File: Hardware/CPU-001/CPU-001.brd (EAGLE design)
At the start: 39.4 x 39.4 mm, 73 parts, among them IC1 IS42S16800F-7TL, J1 10144517-042802LF, J2 10144518-041802LF, J3 10144517-042802LF, J4 10144518-041802LF, J6 2X5_0.05_SWD, U1 ATSAMV71Q19B-AABT, U2 ATA6561-GAQW-N, U6 NCV8170AXV330T2G, U7 ATA6561-GAQW-N

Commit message: more work on CPU-001
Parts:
- added C21: 1uF, rcl:C0603
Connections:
- removed net +3.5V: C1.1, J3.31, J3.33, J3.35, J3.37, J4.31, J4.33, J4.35, J4.37, U6.1, U6.6
- removed net CAN2_N: R39.1, U2.6
- removed net CAN2_P: R39.2, U2.7
- removed net CANRX2: U2.4
- removed net CANTX2: U2.1
- removed net CAN_N: J1.6, J2.6
- removed net CAN_P: J1.4, J2.4
- removed net CAN_STBY2: U2.8
- removed net RFU_3: J1.3, J2.3
- removed net RFU_5: J1.5, J2.5
- removed net RFU_7: J1.7, J2.7
- new net +12V: J3.17, J3.19, J3.21, J3.23, J3.25, J3.27, J3.29, J4.17, J4.19, J4.21, J4.23, J4.25, J4.27, J4.29
- new net CAN0_N: J1.6, J2.6, R26999.1, U7.6
- new net CAN0_P: J1.4, J2.4, R26999.2, U7.7
- new net CANRX0: U7.4
- new net CANTX0: U7.1
- new net CAN_STBY0: U7.8
- net +3V3: now also C21.1, U$5.4
- net +5V: now also C1.1, J3.31, J3.33, J3.35, J3.37, J4.31, J4.33, J4.35, J4.37, U6.1, U6.6; no longer J3.17, J3.19, J3.21, J3.23, J3.25, J3.27, J3.29, J4.17, J4.19, J4.21, J4.23, J4.25, J4.27, J4.29
- net CAN1_N: now also J1.5, J2.5, R39.1, U2.6; no longer R26999.1, U7.6
- net CAN1_P: now also J1.3, J2.3, R39.2, U2.7; no longer R26999.2, U7.7
- net CANRX1: now also U2.4; no longer U7.4
- net CANTX1: now also U2.1; no longer U7.1
- net CAN_STBY1: now also U2.8; no longer U7.8
- net GND: now also C21.2, U$5.6, U$5.MT1, U$5.MT2
- net PA25: now also U$5.5
- net PA26: now also U$5.1
- net PA27: now also U$5.2
- net PA28: now also U$5.3
- net PA30: now also U$5.7
- net PA31: now also U$5.8
- net SHIELD: now also J1.7, J2.7
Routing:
- net CAN_P: track 9.77 -> 0.00 mm, vias 1 -> 0
- net CAN_N: track 9.57 -> 0.00 mm, vias 1 -> 0
- net CAN0_P: track 0.00 -> 8.20 mm, vias 0 -> 1
- net CAN0_N: track 0.00 -> 8.00 mm, vias 0 -> 1
- net RFU_7: track 3.07 -> 0.00 mm, vias 1 -> 0
- net RFU_5: track 3.07 -> 0.00 mm, vias 1 -> 0
- net RFU_3: track 3.07 -> 0.00 mm, vias 1 -> 0
- net CAN1_P: track 0.00 -> 1.44 mm, vias 0 -> 1
- net CAN1_N: track 0.00 -> 1.44 mm, vias 0 -> 1

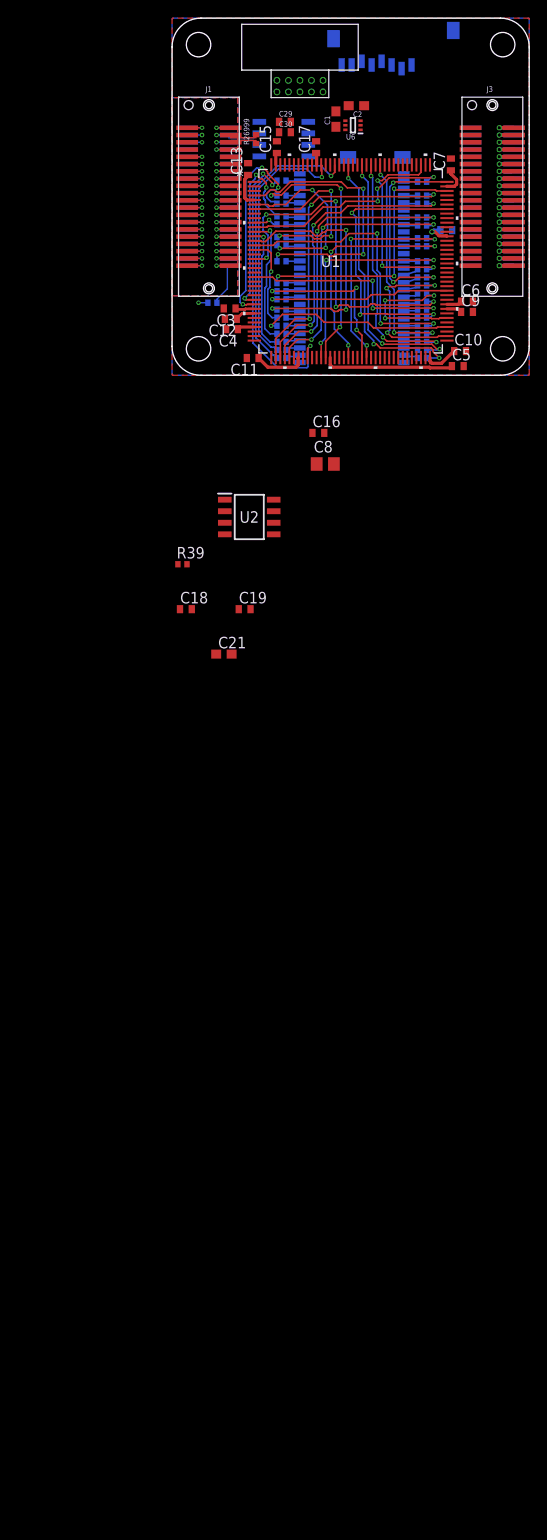
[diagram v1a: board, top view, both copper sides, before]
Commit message: added altimeter.. working through schematic slowly...
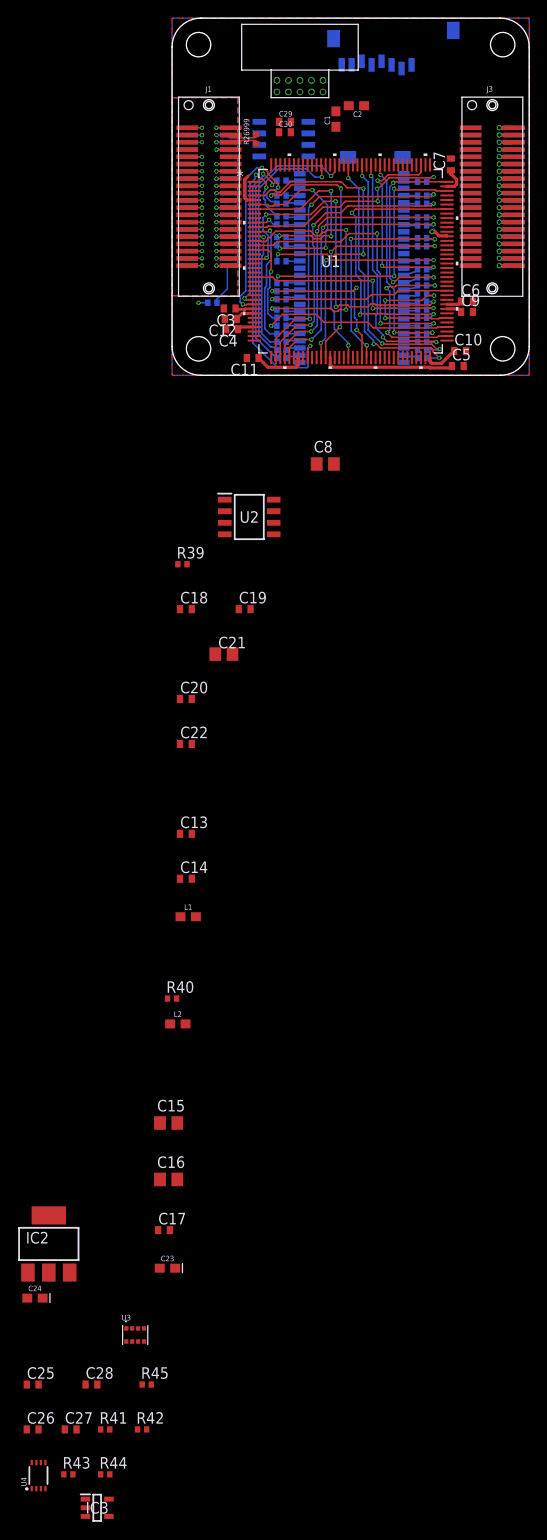
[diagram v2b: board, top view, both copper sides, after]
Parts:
- removed U6: NCV8170AXV330T2G, SamacSys_Parts:SOTFL50P160X60-6N
- added C20: 1u, rcl:C0402
- added C22: 100n, rcl:C0402
- added C23, C24: 10uF, SparkFun-Capacitors:0603-POLAR
- added C25, C28: 100nF, rcl:C0402
- added C26, C27: 1uF, rcl:C0402
- added IC2: NCV1117ST33T3G, v-reg:SOT223
- added IC3: TLV71318PQDBVRQ1, SamacSys_Parts:SOT95P280X100-5N
- added L1, L2: 470@100MHz, SparkFun-Coils:0603
- added R40, R43, R44: (no value), rcl:R0402
- added R41, R42: 10k, rcl:R0402
- added R45: 200k, rcl:R0402
- added U3: ICP-10111, ICP-10111:PSON65P250X200X100-8N
- added U4: PCA9306, SparkFun-IC-Comms:PCA9306DC
- C15, C16: value 100n -> 4.7u; device rcl:C0402 -> rcl:C0805
- C21: value 1uF -> 4.7u; device rcl:C0603 -> rcl:C0805
- C8: value 10u -> 4.7u
- moved C17 120.6 mm to (-0.89, -94.2), turned to 0 degrees
- moved C15 108.2 mm to (-0.38, -82.4), turned to 0 degrees
- moved C16 83.9 mm to (-0.38, -88.6)
- moved C14 77.0 mm to (1.52, -55.5), flipped to the top, turned to 0 degrees
- moved C13 73.6 mm to (1.52, -50.5), turned to 0 degrees
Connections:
- removed net CANRX0: U7.4
- removed net CANRX1: U2.4
- removed net CANTX0: U7.1
- removed net CANTX1: U2.1
- removed net CAN_STBY0: U7.8
- removed net CAN_STBY1: U2.8
- removed net N$2: C3.1, C4.1, C5.1, C6.1, C7.1, U1.107, U1.29, U1.33, U1.50, U1.81
- removed net N$3: C10.1, C11.1, C12.1, C13.1, C14.1, C15.1, C16.1, C17.1, C8.1, C9.1, U1.134, U1.143, U1.30, U1.43, U1.5, U1.72, U1.80, U1.96
- removed net VDDTUMIC: U1.139
- new net +1.8V: C25.1, C27.1, IC3.4, IC3.5, R41.2, R42.2, U3.8, U4.1
- new net N$1: C28.1, R45.2, U4.7, U4.8
- new net N$4: L2.1, R40.2
- new net SCL0_1V8: R42.1, U3.4, U4.2
- new net SDA0_1V8: R41.1, U3.3, U4.3
- new net VDDOUT: C17.1, C20.1, C22.1, C3.1, C4.1, C5.1, C6.1, C7.1, L1.1, U1.107, U1.139, U1.29, U1.3, U1.33, U1.50, U1.81
- new net VDDPLLUSB: C16.1, L2.2, U1.143
- net +3V3: now also C10.1, C11.1, C12.1, C13.1, C14.1, C23.+, C26.1, C8.1, C9.1, IC2.4, IC3.1, IC3.3, R40.1, R43.2, R44.2, R45.1, U1.134, U1.30, U1.43, U1.5, U1.72, U1.80, U1.96; no longer U6.3
- net +5V: now also C24.+, IC2.3; no longer U6.1, U6.6
- net GND: now also C20.2, C22.2, C23.-, C24.-, C25.2, C26.2, C27.2, C28.2, IC2.1, IC3.2, U3.1, U3.2, U3.5, U3.6, U3.7, U4.4; no longer U6.2, U6.5
- net PA1: now also U7.8
- net PA2: now also U2.8
- net PA3: now also R43.1, U4.5
- net PA4: now also R44.1, U4.6
- net PB2: now also U7.1
- net PB3: now also U7.4
- net PC12: now also U2.4
- net PC14: now also U2.1
- net VDDPLL: now also C15.1, L1.2
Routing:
- net VDDOUT: track 0.00 -> 23.1 mm
- net N$2: track 23.1 -> 0.00 mm
- net N$3: track 22.7 -> 0.00 mm, vias 1 -> 0
- net +3V3: track 0.00 -> 19.2 mm, vias 0 -> 1

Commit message: updates to CPU-001 and DBG-001
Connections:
- net +3V3: now also IC1.1, IC1.14, IC1.27, IC1.3, IC1.43, IC1.49, IC1.9
- net GND: now also IC1.12, IC1.28, IC1.41, IC1.46, IC1.52, IC1.54, IC1.6
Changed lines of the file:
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@@
 <contactref element="C27" pad="2"/>
 <contactref element="C28" pad="2"/>
+<contactref element="IC1" pad="6"/>
+<contactref element="IC1" pad="12"/>
+<contactref element="IC1" pad="54"/>
+<contactref element="IC1" pad="28"/>
+<contactref element="IC1" pad="41"/>
+<contactref element="IC1" pad="46"/>
+<contactref element="IC1" pad="52"/>
 <wire x1="-9.555" y1="-124.841" x2="-13.962" y2="-122.7312" width="0" layer="19" extent="1-1"/>
 <wire x1="-14.717" y1="-116.205" x2="-13.962" y2="-122.7312" width="0" layer="19" extent="1-1"/>
@@
 <wire x1="5.809" y1="-14.986" x2="8.651" y2="-25.781" width="0" layer="19" extent="1-1"/>
 <wire x1="17.841" y1="-9.779" x2="5.809" y2="-14.986" width="0" layer="19" extent="1-1"/>
-<wire x1="14.435" y1="1.9558" x2="17.841" y2="-9.779" width="0" layer="19" extent="1-1"/>
-<wire x1="8.24" y1="1.905" x2="14.435" y2="1.9558" width="0" layer="19" extent="1-1"/>
+<wire x1="14.084" y1="1.411" x2="17.841" y2="-9.779" width="0" layer="19" extent="1-16"/>
+<wire x1="14.435" y1="1.9558" x2="14.084" y2="1.411" width="0" layer="19" extent="1-16"/>
+<wire x1="8.24" y1="1.905" x2="14.084" y2="1.411" width="0" layer="19" extent="1-16"/>
 <wire x1="5.954" y1="5.08" x2="8.24" y2="1.905" width="0" layer="19" extent="1-1"/>
 <wire x1="5.827" y1="6.223" x2="5.954" y2="5.08" width="0" layer="19" extent="1-1"/>
@@
 <wire x1="30.734" y1="23.891" x2="36.068" y2="24.085" width="0" layer="19" extent="1-1"/>
 <wire x1="25.435" y1="23.1902" x2="30.734" y2="23.891" width="0" layer="19" extent="1-1"/>
-<wire x1="30.3022" y1="14.823" x2="36.068" y2="14.485" width="0" layer="19" extent="1-1"/>
+<wire x1="25.54" y1="18.211" x2="25.435" y2="23.1902" width="0" layer="19" extent="1-16"/>
+<wire x1="25.54" y1="13.411" x2="25.54" y2="18.211" width="0" layer="19" extent="16-16"/>
+<wire x1="30.3022" y1="14.823" x2="25.54" y2="13.411" width="0" layer="19" extent="1-16"/>
 <wire x1="19.47" y1="29.718" x2="25.435" y2="23.1902" width="0" layer="19" extent="1-1"/>
 <wire x1="18.0594" y1="29.0948" x2="19.47" y2="29.718" width="0" layer="19" extent="1-1"/>
@@
 <wire x1="15.435" y1="23.1902" x2="15.019" y2="26.67" width="0" layer="19" extent="1-16"/>
 <wire x1="13.935" y1="23.1902" x2="15.435" y2="23.1902" width="0" layer="19" extent="1-1"/>
+<wire x1="14.084" y1="22.211" x2="13.935" y2="23.1902" width="0" layer="19" extent="1-16"/>
+<wire x1="14.084" y1="20.611" x2="14.084" y2="22.211" width="0" layer="19" extent="16-16"/>
+<wire x1="14.084" y1="15.811" x2="14.084" y2="20.611" width="0" layer="19" extent="16-16"/>
+<wire x1="14.084" y1="11.811" x2="14.084" y2="15.811" width="0" layer="19" extent="16-16"/>
 <wire x1="20.899" y1="34.6112" x2="19.47" y2="29.718" width="0" layer="19" extent="1-16"/>
 <wire x1="17.799" y1="37.1112" x2="20.899" y2="34.6112" width="0" layer="19" extent="16-16"/>
@@
 <contactref element="R44" pad="2"/>
 <contactref element="R45" pad="1"/>
+<contactref element="IC1" pad="27"/>
+<contactref element="IC1" pad="1"/>
+<contactref element="IC1" pad="3"/>
+<contactref element="IC1" pad="9"/>
+<contactref element="IC1" pad="14"/>
+<contactref element="IC1" pad="49"/>
+<contactref element="IC1" pad="43"/>
 <wire x1="-9.555" y1="-123.891" x2="-9.555" y2="-125.791" width="0" layer="19" extent="1-1"/>
 <wire x1="-10.93" y1="-121.158" x2="-9.555" y2="-123.891" width="0" layer="19" extent="1-1"/>
@@
 <wire x1="13.935" y1="1.9558" x2="15.941" y2="-9.779" width="0" layer="19" extent="1-1"/>
 <wire x1="9.0678" y1="6.823" x2="9.54" y2="1.905" width="0" layer="19" extent="1-1"/>
-<wire x1="9.0678" y1="19.323" x2="9.0678" y2="6.823" width="0" layer="19" extent="1-1"/>
+<wire x1="14.084" y1="13.411" x2="9.0678" y2="6.823" width="0" layer="19" extent="1-16"/>
+<wire x1="14.084" y1="18.211" x2="14.084" y2="13.411" width="0" layer="19" extent="16-16"/>
+<wire x1="9.0678" y1="19.323" x2="14.084" y2="18.211" width="0" layer="19" extent="1-16"/>
 <wire x1="9.619" y1="24.13" x2="8.382" y2="21.955075" width="0" layer="19" extent="1-16"/>
 <wire x1="11.796" y1="26.797" x2="9.619" y2="24.13" width="0" layer="19" extent="1-16"/>
 <wire x1="11.557" y1="31.242" x2="11.796" y2="26.797" width="0" layer="19" extent="1-1"/>
-<wire x1="15.935" y1="23.1902" x2="11.796" y2="26.797" width="0" layer="19" extent="1-1"/>
+<wire x1="15.935" y1="23.1902" x2="14.084" y2="18.211" width="0" layer="19" extent="1-16"/>
 <wire x1="21.17" y1="29.718" x2="15.935" y2="23.1902" width="0" layer="19" extent="1-1"/>
 <wire x1="23.099" y1="34.6112" x2="21.17" y2="29.718" width="0" layer="19" extent="1-16"/>
-<wire x1="28.435" y1="1.9558" x2="13.935" y2="1.9558" width="0" layer="19" extent="1-1"/>
-<wire x1="31.862" y1="6.985" x2="31.1" y2="2.667" width="0" layer="19" extent="1-1"/>
-<wire x1="30.3022" y1="15.323" x2="30.3022" y2="7.323" width="0" layer="19" extent="1-1"/>
+<wire x1="25.54" y1="22.211" x2="21.17" y2="29.718" width="0" layer="19" extent="1-16"/>
+<wire x1="25.54" y1="20.611" x2="25.54" y2="22.211" width="0" layer="19" extent="16-16"/>
+<wire x1="25.54" y1="15.811" x2="25.54" y2="20.611" width="0" layer="19" extent="16-16"/>
+<wire x1="28.65311875" y1="15.8115" x2="25.54" y2="15.811" width="0" layer="19" extent="16-16"/>
+<wire x1="25.54" y1="11.811" x2="25.54" y2="15.811" width="0" layer="19" extent="16-16"/>
+<wire x1="30.3022" y1="7.323" x2="25.54" y2="11.811" width="0" layer="19" extent="1-16"/>
+<wire x1="31.1" y1="2.667" x2="31.862" y2="6.985" width="0" layer="19" extent="1-1"/>
+<wire x1="25.54" y1="1.411" x2="28.435" y2="1.9558" width="0" layer="19" extent="1-16"/>
 </signal>
 <signal name="P_GOOD">
